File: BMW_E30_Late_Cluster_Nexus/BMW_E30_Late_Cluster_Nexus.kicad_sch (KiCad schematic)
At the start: 28 parts, among them J1 Blue, J2 White, J3 Yellow, J4 Speedometer, J5 SI Connector, J6 Tachometer, U1 Coolant Temp, U2 Fuel Gauge

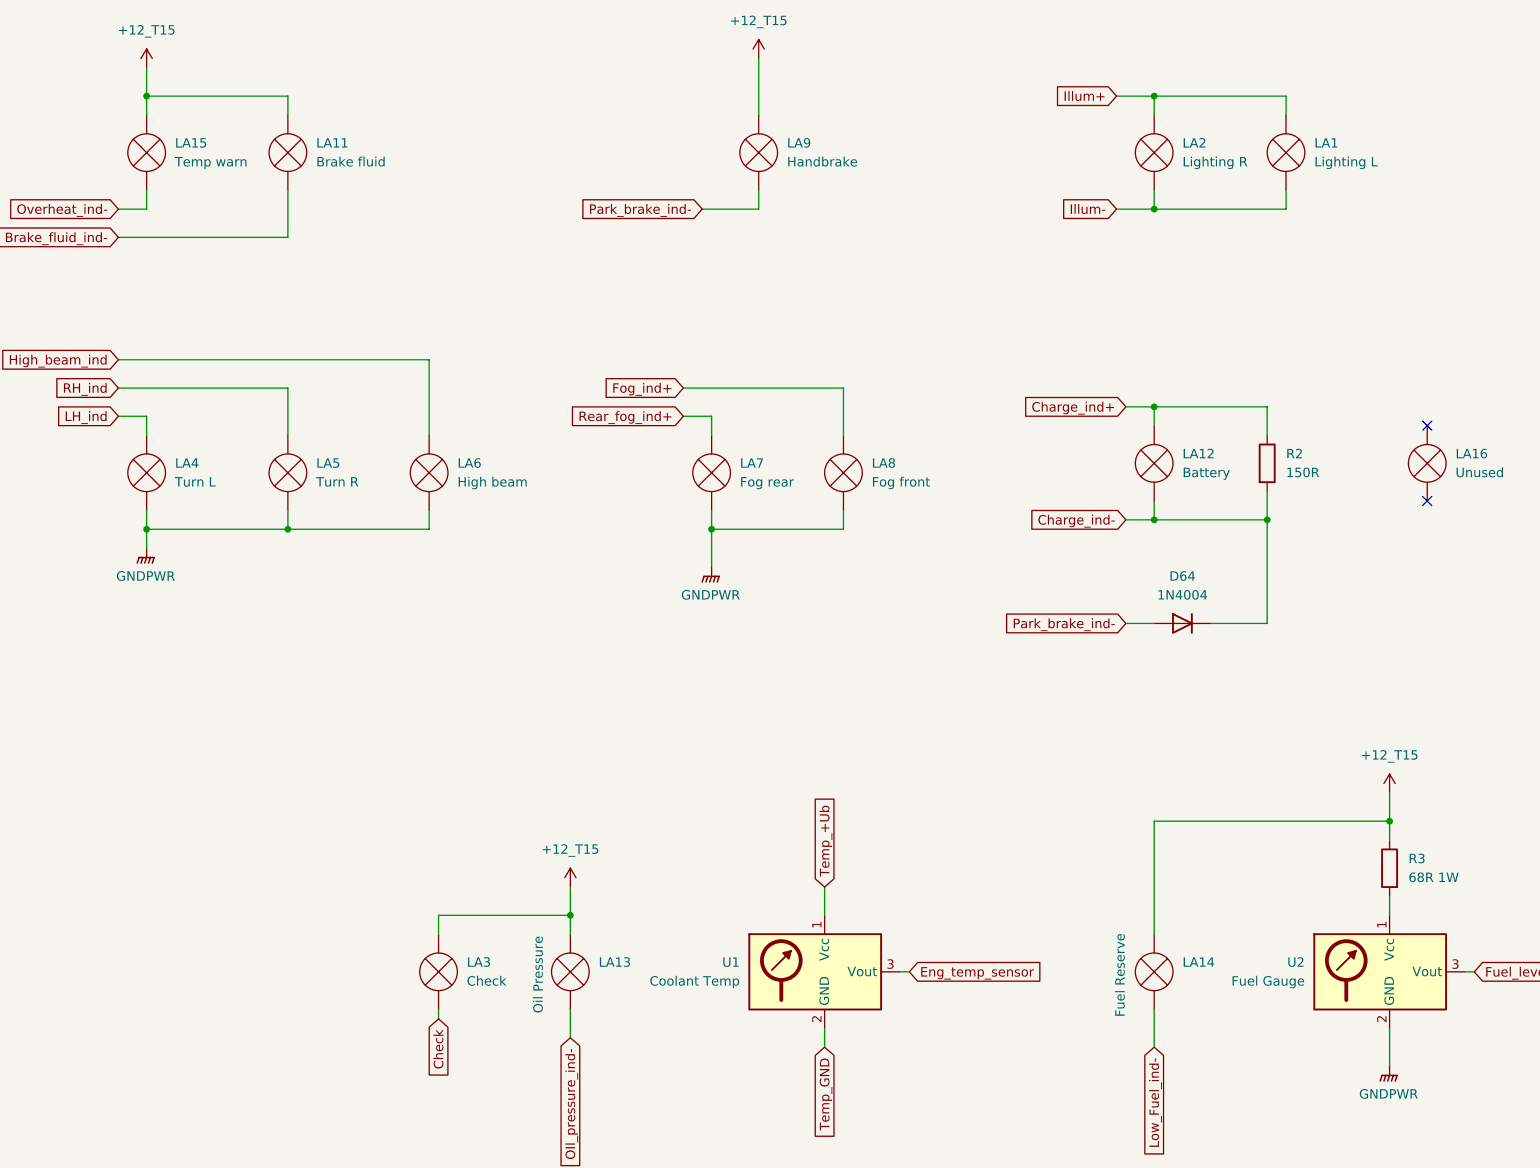
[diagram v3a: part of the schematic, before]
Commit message: Nexus Layout Updates
Layout is about 50% complete. Need to verify exact component locations with early model board.
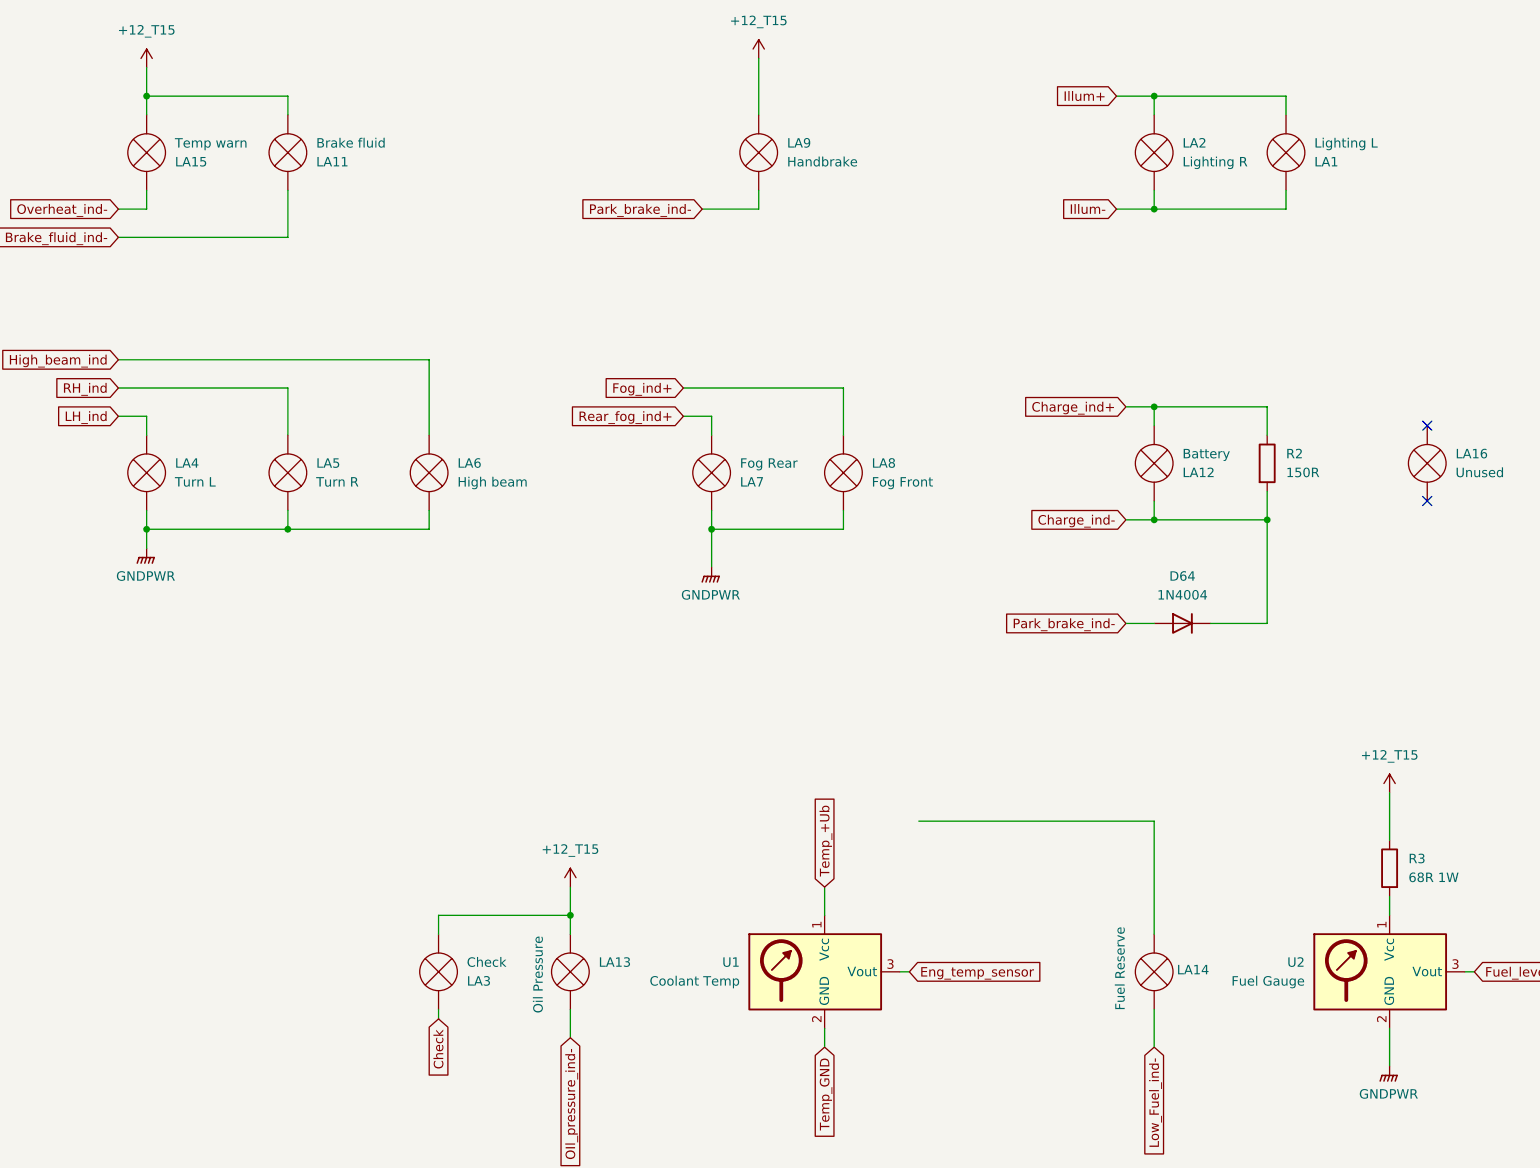
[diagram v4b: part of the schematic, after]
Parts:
- LA7: value Fog rear -> Fog Rear
- LA8: value Fog front -> Fog Front
- U1: footprint BMW_Cluster_Connectors:Gauge_fuel_temp -> BMW_Cluster_Connectors:Gauge_Temp
- U2: footprint BMW_Cluster_Connectors:Gauge_fuel_temp -> BMW_Cluster_Connectors:Gauge_Fuel
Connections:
- net +12_T15: now also LA11.2 (+), LA15.1 (-), LA3.1 (-); no longer LA11.1 (-), LA14.2 (+), LA15.2 (+), LA3.2 (+)
- net Brake_fluid_ind-: now also LA11.1 (-); no longer LA11.2 (+)
- net Charge_ind+: now also LA12.1 (-); no longer LA12.2 (+)
- net Charge_ind-: now also LA12.2 (+); no longer LA12.1 (-)
- net Check: now also LA3.2 (+); no longer LA3.1 (-)
- net GNDPWR: now also LA7.1 (-); no longer LA7.2 (+)
- net Illum+: now also LA1.2 (+); no longer LA1.1 (-)
- net Illum-: now also LA1.1 (-); no longer LA1.2 (+)
- net Low_Fuel_ind-: now also LA14.2 (+); no longer LA14.1 (-)
- net Overheat_ind-: now also LA15.2 (+); no longer LA15.1 (-)
- net Rear_fog_ind+: now also LA7.2 (+); no longer LA7.1 (-)
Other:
- moved on the sheet: LA1, LA11, LA7

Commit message: Layout Updates to Match Early
Changed a few light bulb component locations to match the correct locations on the early model boards.
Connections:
- net +12_T15: now also LA14.1 (-)
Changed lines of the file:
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@@
+	)
+	(junction
+		(at 375.92 153.67)
+		(diameter 0)
+		(color 0 0 0 0)
 	)
 	(junction
@@
 	(wire
 		(pts
-			(xy 375.92 149.86) (xy 375.92 156.21)
+			(xy 375.92 149.86) (xy 375.92 153.67)
 		)
 		(stroke
@@
 	(wire
 		(pts
-			(xy 344.17 153.67) (xy 312.42 153.67)
-		)
-		(stroke
-			(width 0)
-			(type default)
-		)
-	)
-	(wire
-		(pts
 			(xy 62.23 97.79) (xy 67.31 97.79)
 		)
@@
 	(wire
 		(pts
+			(xy 375.92 153.67) (xy 375.92 156.21)
+		)
+		(stroke
+			(width 0)
+			(type default)
+		)
+	)
+	(wire
+		(pts
 			(xy 386.08 173.99) (xy 387.35 173.99)
 		)
@@
 		)
 		(stroke
+			(width 0)
+			(type default)
+		)
+	)
+	(wire
+		(pts
+			(xy 344.17 153.67) (xy 375.92 153.67)
+		)
+		(stroke

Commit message: Added Project Files + Updates
Added project files for SI LED daughter board and speedometer board. Started on reverse engineering schematic for late model SI board.

Also updated some formatting on the nexus board schematic.
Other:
- company: (none) -> Reagan Ansel
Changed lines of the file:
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@@
 	(title_block
 		(title "BMW E30 Late Model Cluster Nexus")
+		(date "2025-11-10")
+		(rev "0")
+		(company "Reagan Ansel")
 	)
 	(junction
@@
 				)
 			)
-			(table_cell "This Schematic Notation"
+			(table_cell "Function"
 				(exclude_from_sim no)
 				(at 124.46 20.32 0)
